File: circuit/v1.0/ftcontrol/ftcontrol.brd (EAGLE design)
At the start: 55.9 x 55.9 mm, 28 parts, among them IC1 7805, IC2 7805, IC3 ATMEGA328P-PU, IC4 L293D, J3 ISP, J4 SERVO, J5 PING, J6 MOTORS, Q1 16Mhz

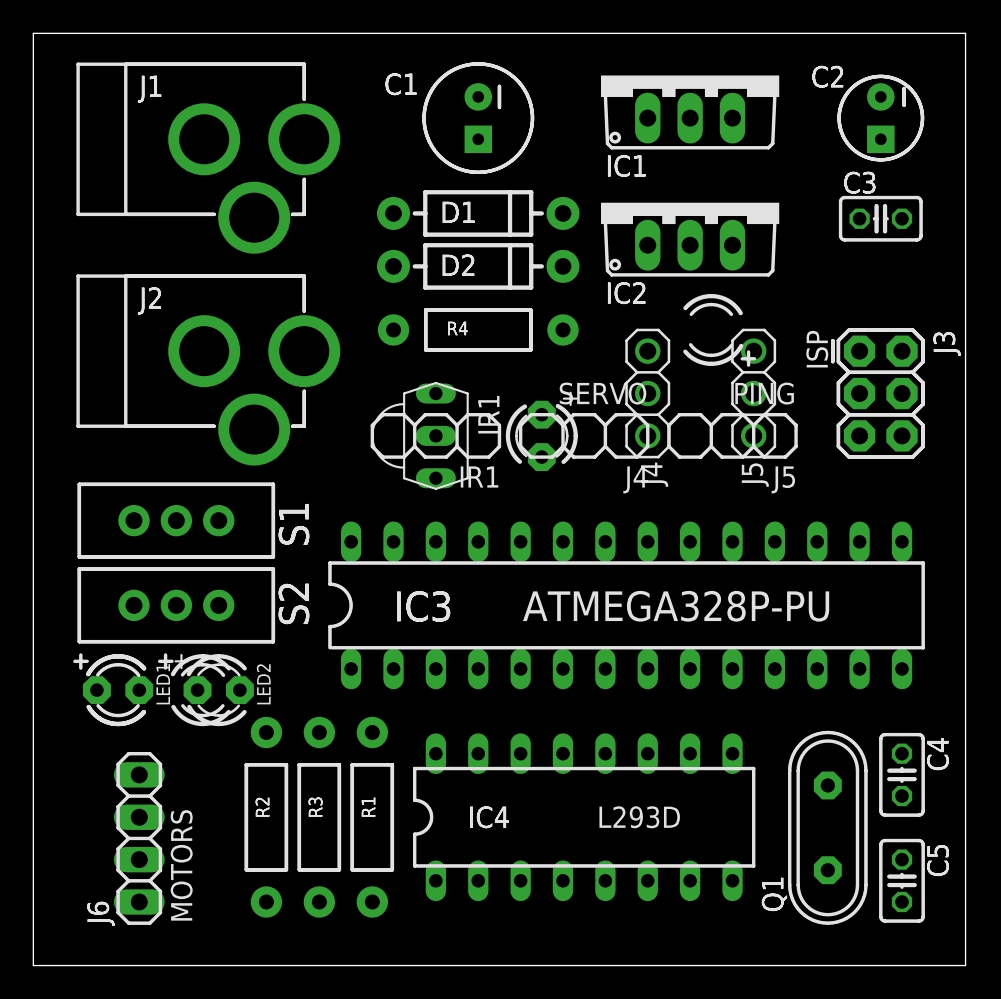
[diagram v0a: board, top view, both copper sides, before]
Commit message: moved servo/ping connectors
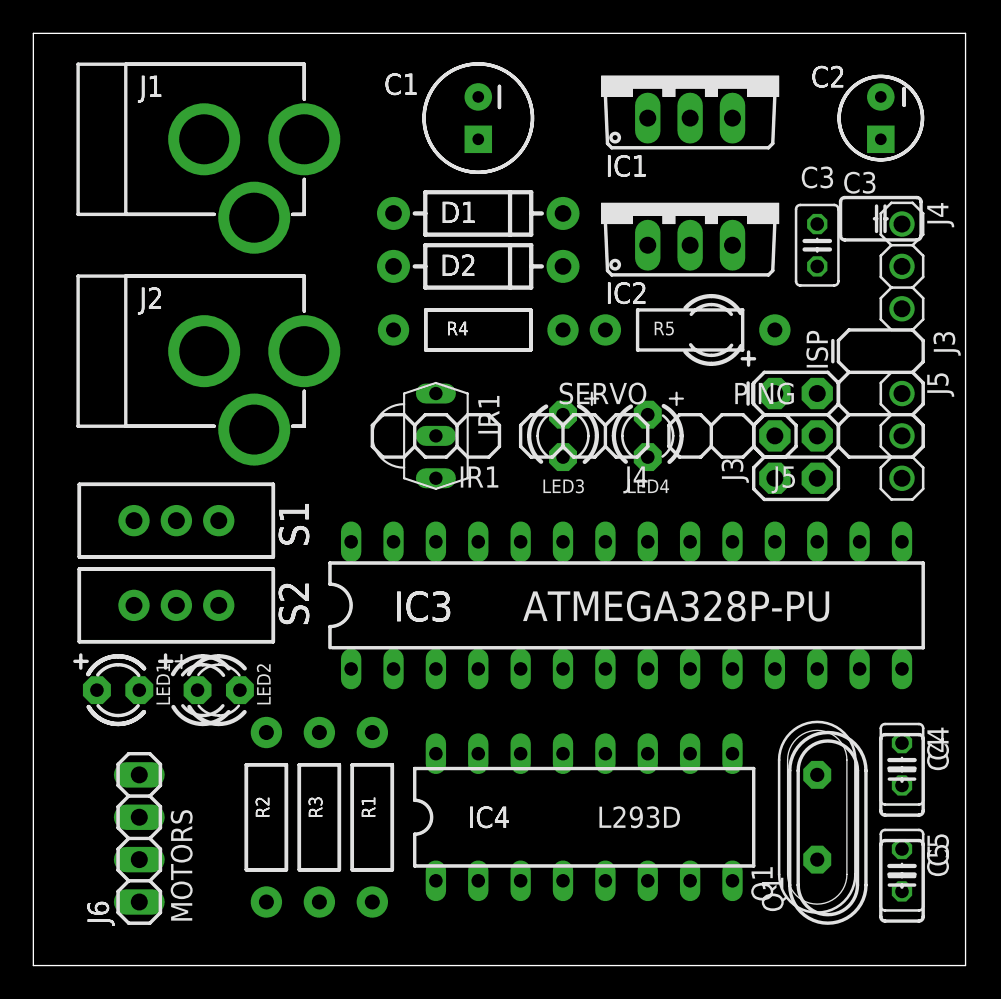
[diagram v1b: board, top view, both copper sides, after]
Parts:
- added LED4: (no value), adafruit:LED3MM
- added R5: 1K, SparkFun-Resistors:AXIAL-0.4
- moved J4 17.0 mm to (52.1, 64.8)
- moved J5 9.25 mm to (52.1, 54.6)
- moved J3 5.68 mm to (44.5, 57.1)
- moved C3 4.13 mm to (47.0, 66.0), turned to 270 degrees
- moved LED3 1.27 mm to (31.8, 54.6)
- moved Q1 0.90 mm to (47.0, 31.8)
- moved C4 0.63 mm to (52.1, 34.9)
- moved C5 0.63 mm to (52.1, 28.6)
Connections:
- new net N$9: LED4.K, R5.P$2
- net GND: now also R5.P$1
- net PD0: now also LED4.A

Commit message: imported firmware
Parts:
- moved IR1 1.27 mm to (24.1, 55.9), turned to 0 degrees
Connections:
- removed net N$2: C1.1, D1.C, IC1.1
- removed net PD2: IC3.4
- removed net PD5: IC3.11
- new net N$13: J1.PWR, S1.2
- net GND: now also J1.GND, J2.GND; no longer J1.PWR, J2.PWR
- net N$5: now also J2.PWR, S2.2; no longer D2.C, IC2.1
- net VCC: now also C1.1, D1.C, IC1.1; no longer J1.GND, S1.2
- net VCC/2: now also D2.C, IC2.1; no longer J2.GND, S2.2
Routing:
- net GND: track 0.00 -> 223.7 mm
- net 5V: track 0.00 -> 142.4 mm
- net 5V/SERVO: track 0.00 -> 61.7 mm
- net VCC/2: track 0.00 -> 46.1 mm
- net 3Y: track 0.00 -> 45.6 mm
- net PB0: track 0.00 -> 43.0 mm, vias 0 -> 1
- net 4Y: track 0.00 -> 37.7 mm
- net N$3: track 0.00 -> 37.2 mm
- net PC6: track 0.00 -> 36.1 mm
- net 2Y: track 0.00 -> 33.1 mm
- net N$11: track 0.00 -> 30.7 mm
- net PD0: track 0.00 -> 29.9 mm, vias 0 -> 1
- net 1Y: track 0.00 -> 27.0 mm
- net N$13: track 0.00 -> 26.8 mm
- net PD6: track 0.00 -> 25.9 mm
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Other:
- board text added: "LED1"
- board text added: "LED2"
- board text added: "LED3"
- board text added: "LED4"
- board text added: "R5"
